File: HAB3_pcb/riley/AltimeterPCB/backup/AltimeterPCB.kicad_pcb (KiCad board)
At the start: 4 copper layers, 4 parts, among them U1 MS560702BA03-00

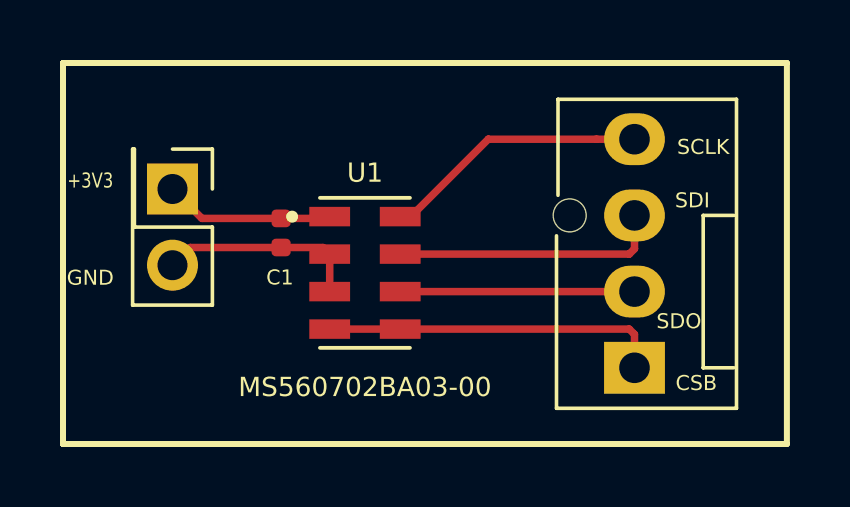
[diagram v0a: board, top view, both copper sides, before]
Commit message: updated labels on riley's pcb
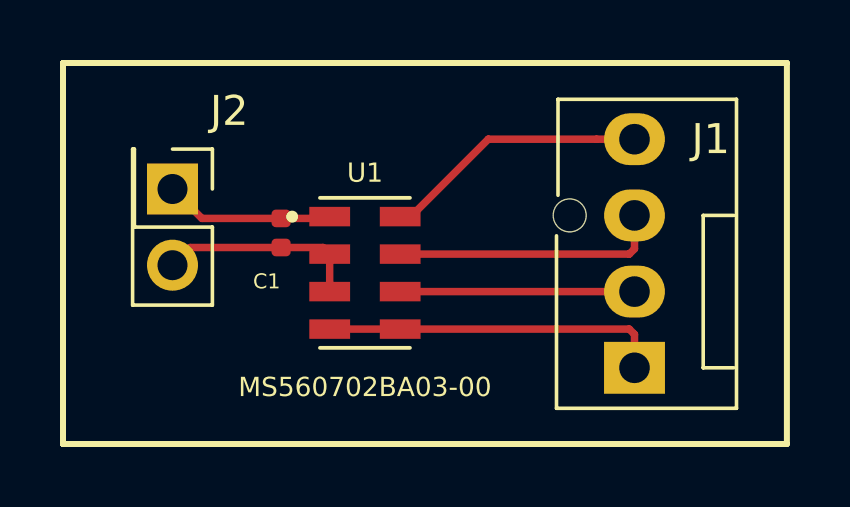
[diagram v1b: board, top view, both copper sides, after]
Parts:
- J1: renamed from ?; value (none) -> Conn_01x04_Female
- J2: renamed from ?; value (none) -> Conn_02x01
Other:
- copper layers 4 -> 2
- board text removed: "+3V3"
- board text removed: "CSB"
- board text removed: "GND"
- board text removed: "SCLK"
- board text removed: "SDI"
- board text removed: "SDO"
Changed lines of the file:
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@@
   (general
     (thickness 1.6)
-    (drawings 12)
+    (drawings 6)
     (tracks 21)
     (zones 0)
@@
   (layers
     (0 F.Cu signal)
-    (1 In1.Cu power)
-    (2 In2.Cu power)
     (31 B.Cu signal)
     (32 B.Adhes user)
@@
     (descr "4-pin CPU fan Through hole pin header, e.g. for Wieson part number 2366C888-007 Molex 47053-1000, Foxconn HF27040-M1, Tyco 1470947-1 or equivalent, see http://www.formfactors.org/developer%5Cspecs%5Crev1_2_public.pdf")
     (tags "pin header 4-pin CPU fan")
-    (fp_text reference "" (at 5.91 2.06) (layer F.SilkS) hide
-      (effects (font (size 1 1) (thickness 0.15)))
-    )
-    (fp_text value "" (at 3.83 4.21 90) (layer F.Fab) hide
+    (fp_text reference J1 (at 7.62 2.54) (layer F.SilkS)
+      (effects (font (size 1 1) (thickness 0.15)))
+    )
+    (fp_text value Conn_01x04_Female (at 3.83 4.21 90) (layer F.Fab)
       (effects (font (size 0.5 0.5) (thickness 0.125)))
     )
@@
     (tags capacitor)
     (attr smd)
-    (fp_text reference C1 (at 1.485 0.04) (layer F.SilkS)
+    (fp_text reference C1 (at 1.615 0.48) (layer F.SilkS)
       (effects (font (size 0.5 0.5) (thickness 0.125)))
     )
@@
     (descr "Through hole straight pin header, 2x01, 2.54mm pitch, double rows")
     (tags "Through hole pin header THT 2x01 2.54mm double row")
-    (fp_text reference "" (at -2.6 -1.89) (layer F.SilkS) hide
-      (effects (font (size 1 1) (thickness 0.15)))
-    )
-    (fp_text value "" (at 1.25 2.57 270) (layer F.Fab)
+    (fp_text reference J2 (at -2.6 -1.89) (layer F.SilkS)
+      (effects (font (size 1 1) (thickness 0.15)))
+    )
+    (fp_text value Conn_02x01 (at 1.25 2.57 270) (layer F.Fab)
       (effects (font (size 1 1) (thickness 0.15)))
     )
@@
     )
   )
-  (gr_text GND (at 117.75 103.68) (layer F.SilkS)
-    (effects (font (size 0.5 0.5) (thickness 0.125)))
-  )
-  (gr_text +3V3 (at 117.75 100.44) (layer F.SilkS)
-    (effects (font (size 0.5 0.4) (thickness 0.075)))
-  )
-  (gr_text CSB (at 137.95 107.19) (layer F.SilkS)
-    (effects (font (size 0.5 0.5) (thickness 0.125)))
-  )
-  (gr_text SDO (at 137.37 105.13) (layer F.SilkS)
-    (effects (font (size 0.5 0.5) (thickness 0.125)))
-  )
-  (gr_text SDI (at 137.82 101.1) (layer F.SilkS)
-    (effects (font (size 0.5 0.5) (thickness 0.125)))
-  )
-  (gr_text SCLK (at 138.18 99.32) (layer F.SilkS)
-    (effects (font (size 0.5 0.5) (thickness 0.125)))
-  )
   (gr_line (start 116.84 109.22) (end 124.46 109.22) (layer F.SilkS) (width 0.2))
